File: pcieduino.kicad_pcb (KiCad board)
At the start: 2 copper layers, 51 x 30 mm, 31 parts, among them IC1 ATMEGA328P-A, J1 PCIE-MINI, J2 DIGITAL2, J3 POWER, J4 ISP, J5 ANALOG, J6 DIGITAL, SW1 SW_PUSH, U1 MCP2200, X1 12MHz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

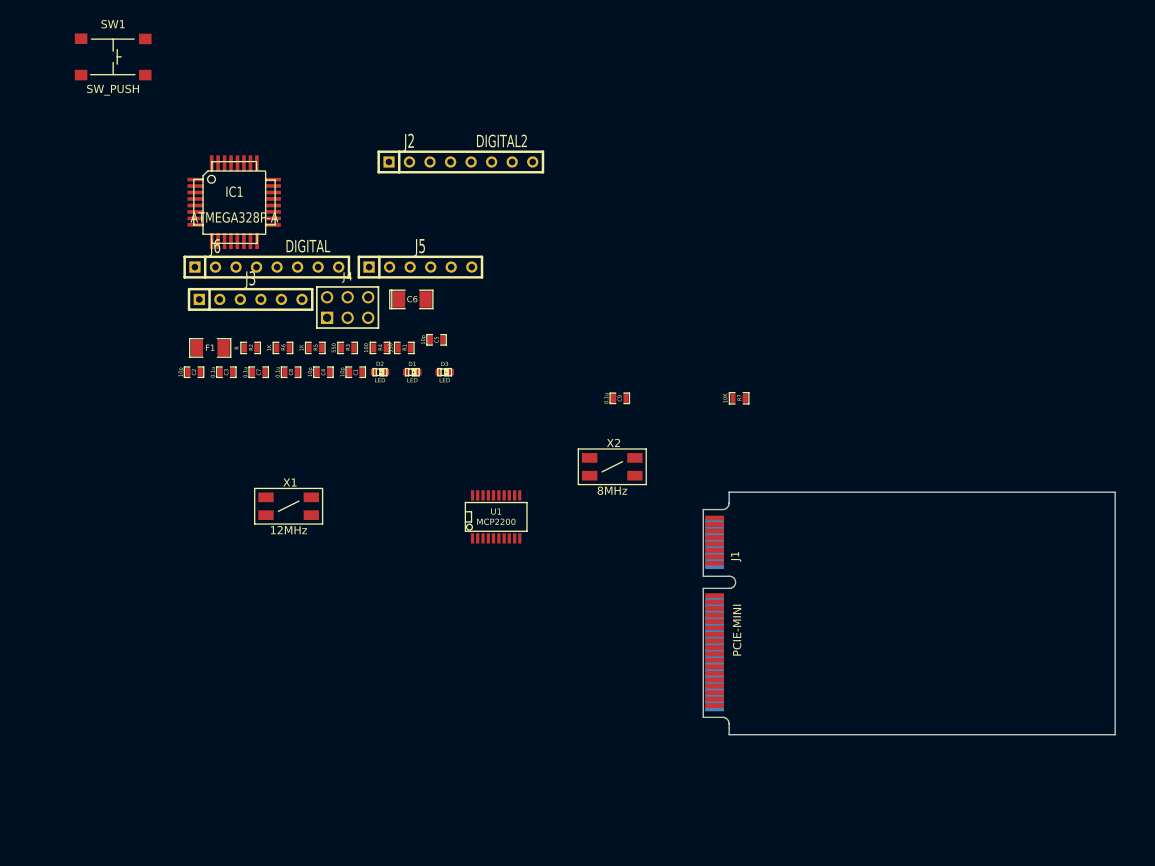
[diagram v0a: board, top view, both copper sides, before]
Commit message: add progress on 01/03
Quick summary:

* new crystal footprint
* new switch footprint
* combining digital pins
* adding mounting holes

... and some small positioning changes
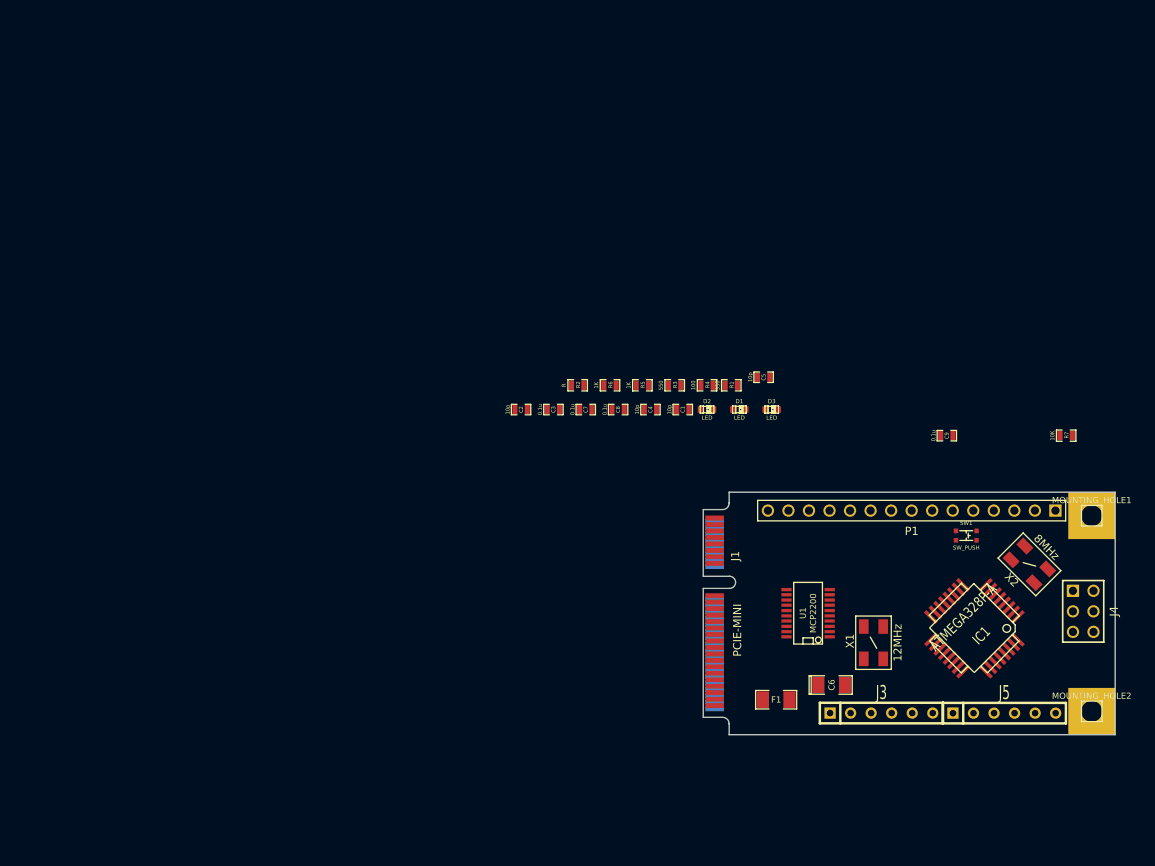
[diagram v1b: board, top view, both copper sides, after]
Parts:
- removed J2: DIGITAL2, SIL-8
- removed J6: DIGITAL, SIL-8
- added MOUNTING_HOLE1: CONN_1, PIN_ARRAY_1, F.Cu at (182.0, 88.8)
- added MOUNTING_HOLE2: CONN_1, PIN_ARRAY_1, F.Cu at (182.0, 113.0)
- added P1: DIGITAL, PIN_ARRAY_15x1, F.Cu at (159.8, 88.1)
- SW1: footprint SWITCH -> SMD_SWITCH
- X1, X2: footprint SMDXTAL -> SMDXTAL_50x32
- moved SW1 121.0 mm to (166.5, 91.2)
- moved IC1 105.6 mm to (167.5, 102.7), turned to 225 degrees
- moved J4 98.4 mm to (181.0, 100.6), turned to 270 degrees
- moved J3 93.3 mm to (156.0, 113.2)
- moved J5 90.9 mm to (171.2, 113.2)
- moved F1 82.4 mm to (143.0, 111.5)
- moved X1 74.3 mm to (155.0, 104.5), turned to 90 degrees
- moved C6 70.5 mm to (149.9, 109.7)
- moved X2 53.0 mm to (174.3, 94.8), turned to 135 degrees
- moved C9 40.7 mm to (164.1, 78.8)
- moved R7 40.7 mm to (178.9, 78.8)
- moved C2 40.7 mm to (111.5, 75.6)
- moved C3 40.7 mm to (115.5, 75.6)
- moved C4 40.7 mm to (127.5, 75.6)
- moved C7 40.7 mm to (119.5, 75.6)
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
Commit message: more progress on 01/03
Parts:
- removed P1: DIGITAL, PIN_ARRAY_15x1
- added J2: ANALOG, pin_array_8x1, F.Cu at (168.8, 113.3)
- J3: value POWER -> ISP; footprint SIL-6 -> pin_array_3x2
- J4: value ISP -> POWER; footprint pin_array_3x2 -> pin_array_6x1
- J5: value ANALOG -> DIGITAL; footprint SIL-6 -> PIN_ARRAY_15x1
- moved C3 56.8 mm to (161.4, 109.0), turned to 180 degrees
- moved C4 54.5 mm to (176.3, 99.8)
- moved R6 46.3 mm to (161.2, 97.9)
- moved C2 46.3 mm to (145.8, 106.6)
- moved C5 45.8 mm to (181.0, 94.8)
- moved C8 43.8 mm to (159.1, 101.0)
- moved R5 42.4 mm to (161.9, 95.9)
- moved C7 41.8 mm to (144.8, 108.9)
- moved C9 36.6 mm to (141.4, 107.5)
- moved C1 36.3 mm to (150.3, 106.7)
- moved R3 36.3 mm to (157.8, 96.6)
- moved R2 35.6 mm to (146.5, 94.7)
- moved R1 33.0 mm to (157.8, 98.7)
- moved J4 32.5 mm to (151.1, 113.3), turned to 0 degrees
- moved D2 29.2 mm to (154.6, 96.7)
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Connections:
- IC1 pad 19: (no net) -> /A6
- IC1 pad 22: (no net) -> /A7
- J3 pad 1: /RESET -> /D12/MISO
- J3 pad 3: VCC -> /D13/SCK
- J3 pad 4: GND -> /D11/MOSI
- J3 pad 5: GND -> /RESET
- J3 pad 6: /AREF -> GND
- J4 pad 1: /D12/MISO -> /RESET
- J4 pad 3: /D13/SCK -> VCC
- J4 pad 4: /D11/MOSI -> GND
- J4 pad 5: /RESET -> GND
- J4 pad 6: GND -> /AREF
- J5 pad 1: /A0 -> N-0000035
- J5 pad 2: /A1 -> N-0000034
- J5 pad 3: /A2 -> /D2
- J5 pad 4: /A3 -> /D3
- J5 pad 5: /A4 -> /D4
- J5 pad 6: /A5 -> /D5
- R5 pad 2: N-0000047 (its old number) -> N-0000035
- R6 pad 2: N-0000048 -> N-0000034
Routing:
- added copper zone on F.Cu, net GND
- added copper zone on B.Cu, net VCC
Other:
- board text added: "CC-BY-SA-3.0"
- board text added: "Moonpunch.org"
- board text added: "PCIeDuino v1"

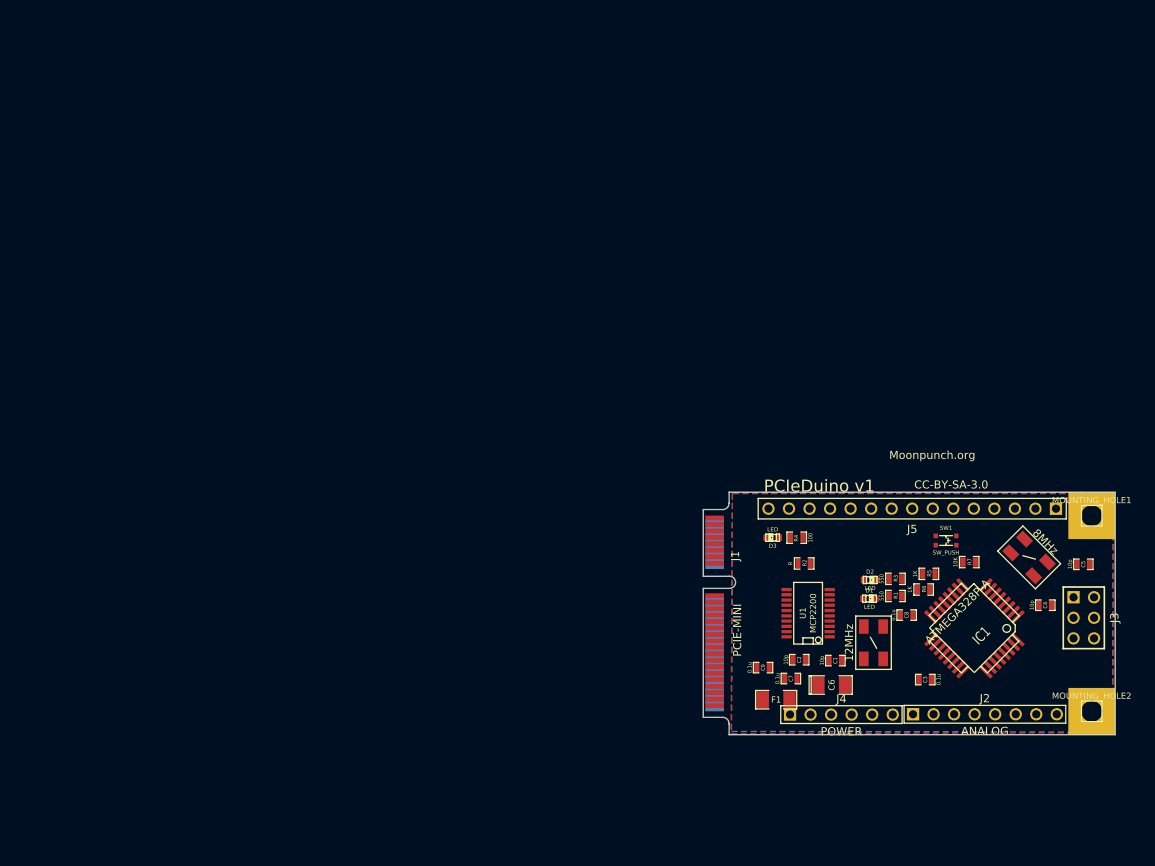
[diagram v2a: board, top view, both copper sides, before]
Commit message: add 01/04 changes
summary:

* redrawn the board starting from x=100.00, y=100.00 to have fix positioning
* combine analog and power headers
* remove RESET from power header because it already exists elsewhere
* redraw fill zones with duplication
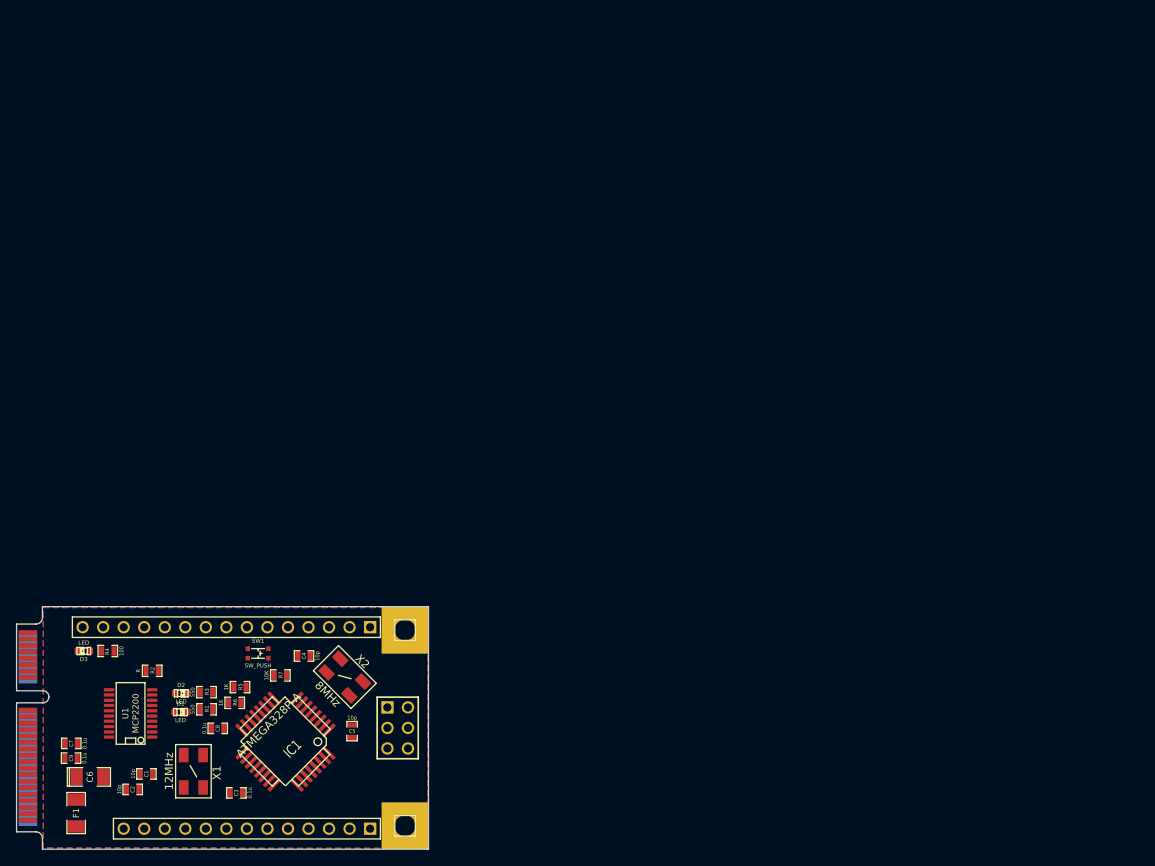
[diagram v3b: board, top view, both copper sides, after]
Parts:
- removed J5: DIGITAL, PIN_ARRAY_15x1
- J2: value ANALOG -> ANALOG_POWER; footprint pin_array_8x1 -> PIN_ARRAY_13x1
- J4: value POWER -> DIGITAL; footprint pin_array_6x1 -> PIN_ARRAY_15x1
- moved C5 92.8 mm to (90.5, 115.4), turned to 270 degrees
- moved C6 92.4 mm to (58.1, 121.1)
- moved J2 92.4 mm to (77.5, 127.5), turned to 180 degrees
- moved C4 91.9 mm to (84.6, 106.1), turned to 180 degrees
- moved C7 89.4 mm to (55.8, 116.9), turned to 180 degrees
- moved F1 87.7 mm to (56.4, 125.5), turned to 90 degrees
- moved R6 86.4 mm to (76.0, 111.9)
- moved C1 86.4 mm to (65.1, 120.7)
- moved C3 86.4 mm to (76.2, 123.0)
- moved D1 86.4 mm to (69.3, 113.0)
- moved D3 86.4 mm to (57.4, 105.5)
- moved IC1 86.4 mm to (82.3, 116.7)
- moved R4 86.4 mm to (60.3, 105.5)
- moved R7 86.4 mm to (81.7, 108.5)
- moved D2 86.4 mm to (69.4, 110.7)
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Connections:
- J2 pad 1: /A0 -> /A7
- J2 pad 2: /A1 -> /A6
- J2 pad 3: /A2 -> /A5
- J2 pad 4: /A3 -> /A4
- J2 pad 5: /A4 -> /A3
- J2 pad 6: /A5 -> /A2
- J2 pad 7: /A6 -> /A1
- J2 pad 8: /A7 -> /A0
- J4 pad 1: /RESET -> N-0000032
- J4 pad 2: VCC -> N-0000031
- J4 pad 3: VCC -> /D2
- J4 pad 4: GND -> /D3
- J4 pad 5: GND -> /D4
- J4 pad 6: /AREF -> /D5
- R5 pad 2: N-0000035 -> N-0000032
- R6 pad 2: N-0000034 -> N-0000031
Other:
- outline, holes or cut-outs redrawn
- net class Default: clearance 0.254 -> 0.2; via_dia 0.889 -> 0.762; via_drill 0.635 -> 0.3048
- net class PCI added: clearance 0.2, trace_width 0.4, via_dia 0.762, via_drill 0.3048
- net class Power added: clearance 0.2, trace_width 0.4, via_dia 0.889, via_drill 0.635
- rule trace_clearance: 0.254 -> 0.2
- rule via_min_drill: 0.508 -> 0.299974
- rule via_min_size: 0.889 -> 0.6
- board text removed: "CC-BY-SA-3.0"
- board text removed: "Moonpunch.org"
- board text removed: "PCIeDuino v1"

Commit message: progres on 01/05: mostly crystal work
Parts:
- X1: value 12MHz -> 12MHZ; footprint SMDXTAL_50x32 -> SMDXTAL_32x25
- moved X1 1.64 mm to (70.0, 119.0), turned to 90 degrees
- moved X2 0.68 mm to (90.2, 109.1), turned to 0 degrees
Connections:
- C1 pad 1: N-0000042 -> N-0000035
- C2 pad 1: N-0000043 (its old number) -> N-0000034
- C4 pad 1: N-000002 -> N-0000041
- C5 pad 1: N-000003 -> N-0000040
- IC1 pad 7: N-000002 -> N-0000041
- IC1 pad 8: N-000003 -> N-0000040
- U1 pad 2: N-0000042 -> N-0000035
- U1 pad 3: N-0000043 (its old number) -> N-0000034
- X1 pad 1: N-0000043 (its old number) -> N-0000035
- X1 pad 2: N-0000042 -> N-0000034
- X2 pad 1: N-000002 -> N-0000040
- X2 pad 2: N-000003 -> N-0000041
